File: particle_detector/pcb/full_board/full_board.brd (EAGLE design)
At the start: 32 x 64 mm, 39 parts, among them IC1 LT1807R, IC2 ATTINY5, IC3 LT3461, IC5 SENSL-SIPM

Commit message: Change ATTiny pads to save space
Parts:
- IC1: device personal:SO8 -> Personal:SO8
- IC2: device personal:PDIP8 -> Personal:PDIP8
- IC3: device personal:SOT23-6 -> Personal:SOT23-6
- IC5: device personal:MICROFC-60035 -> Personal:MICROFC-60035
- XBUS1, XBUS2: device personal:XBUS_2X05_PAD -> Personal:XBUS_2X05_PAD
- moved IC2 0.96 mm to (-8.45, 43.3)
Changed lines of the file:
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@@
 <attribute name="PROD_ID" value="DIO-09886" x="29.65" y="68" size="1.778" layer="27" rot="R90" display="off"/>
 </element>
-<element name="IC1" library="personal" package="SO8" package3d_urn="urn:adsk.eagle:package:3906/1" value="LT1807R" x="21.35" y="59" smashed="yes" rot="R270">
+<element name="IC1" library="Personal" package="SO8" package3d_urn="urn:adsk.eagle:package:3906/1" value="LT1807R" x="21.35" y="59" smashed="yes" rot="R270">
 <attribute name="MF" value="ALTERA CORPORATION" x="21.35" y="59" size="1.778" layer="27" rot="R270" display="off"/>
 <attribute name="MPN" value="AD746JRZ" x="21.35" y="59" size="1.778" layer="27" rot="R270" display="off"/>
@@
 <attribute name="VALUE" x="21.745" y="57.045" size="0.6" layer="27" font="vector" rot="R90"/>
 </element>
-<element name="IC3" library="personal" package="SOT23-6" value="LT3461" x="9.65" y="52.6" smashed="yes" rot="R270">
+<element name="IC3" library="Personal" package="SOT23-6" value="LT3461" x="9.65" y="52.6" smashed="yes" rot="R270">
 <attribute name="VALUE" x="8.095" y="49.421" size="0.6" layer="27" font="vector"/>
 </element>
@@
 <attribute name="VALUE" x="27.94" y="71.28" size="0.6" layer="27" font="vector" rot="R90"/>
 </element>
-<element name="XBUS1" library="personal" package="XBUS_2X05_PAD" value="" x="16" y="46.85" smashed="yes">
+<element name="XBUS1" library="Personal" package="XBUS_2X05_PAD" value="" x="16" y="46.85" smashed="yes">
 <attribute name="VALUE" x="11.92" y="43.675" size="1.27" layer="27"/>
 </element>
-<element name="L1" library="rcl" library_urn="urn:adsk.eagle:library:334" package="L3225M" package3d_urn="urn:adsk.eagle:package:23477/1" value="47uH" x="9.6" y="58.2" smashed="yes" rot="R90">
+<element name="L1" library="rcl" library_urn="urn:adsk.eagle:library:334" package="L3225M" package3d_urn="urn:adsk.eagle:package:23477/2" value="47uH" x="9.6" y="58.2" smashed="yes" rot="R90">
 <attribute name="NAME" x="7.695" y="60.805" size="0.6" layer="25" font="vector"/>
+<attribute name="POPULARITY" value="11" x="9.6" y="58.2" size="1.778" layer="27" rot="R90" display="off"/>
 <attribute name="SPICEPREFIX" value="L" x="9.6" y="58.2" size="1.778" layer="27" rot="R90" display="off"/>
 <attribute name="VALUE" x="8.795" y="60.825" size="0.6" layer="27" font="vector"/>
 </element>
-<element name="IC5" library="personal" package="MICROFC-60035" value="SENSL-SIPM" x="16" y="91.35" smashed="yes" rot="R180"/>
+<element name="IC5" library="Personal" package="MICROFC-60035" value="SENSL-SIPM" x="16" y="91.35" smashed="yes" rot="R180"/>
 <element name="C12" library="rcl" package="C0805K" value="10uF" x="13" y="66" smashed="yes">
 <attribute name="NAME" x="11.2" y="66.975" size="0.6" layer="25" font="vector"/>
@@
 <attribute name="VALUE" x="11.84" y="73.83" size="0.6" layer="27" font="vector" rot="R90"/>
 </element>
-<element name="XBUS2" library="personal" package="XBUS_2X05_PAD" value="" x="28.6" y="59.35" smashed="yes" rot="R270">
+<element name="XBUS2" library="Personal" package="XBUS_2X05_PAD" value="" x="28.6" y="59.35" smashed="yes" rot="R270">
 <attribute name="VALUE" x="25.425" y="63.43" size="1.27" layer="27" rot="R270"/>
 </element>
@@
 <attribute name="VALUE" x="28.33" y="69.825" size="1.27" layer="27"/>
 </element>
-<element name="IC2" library="personal" package="PDIP8" value="ATTINY5" x="-7.7" y="43.9" smashed="yes">
-<attribute name="NAME" x="-10.24" y="51.012" size="1.27" layer="25"/>
-<attribute name="VALUE" x="-10.748" y="35.518" size="1.27" layer="27"/>
+<element name="IC2" library="Personal" package="PDIP8" value="ATTINY5" x="-8.45" y="43.3" smashed="yes">
+<attribute name="NAME" x="-10.99" y="50.412" size="1.27" layer="25"/>
+<attribute name="VALUE" x="-11.498" y="34.918" size="1.27" layer="27"/>
 </element>
 </elements>
@@
 <wire x1="29.75" y1="45.6" x2="27.4" y2="52.8" width="0" layer="19" extent="1-1"/>
 <wire x1="2.25" y1="45.6" x2="8.35" y2="52.6" width="0" layer="19" extent="1-1"/>
-<wire x1="-11.256" y1="40.09" x2="2.25" y2="45.6" width="0" layer="19" extent="1-1"/>
+<wire x1="-12.006" y1="39.49" x2="2.25" y2="45.6" width="0" layer="19" extent="1-1"/>
 <wire x1="2.25" y1="105.1" x2="28" y2="103.35" width="0" layer="19" extent="1-1"/>
 </signal>
@@
 <wire x1="24.6637" y1="48.6637" x2="21.0156" y2="48.6637" width="0.2" layer="1"/>
 <contactref element="IC2" pad="P5"/>
-<wire x1="-3.636" y1="40.09" x2="18" y2="46.85" width="0" layer="19" extent="1-1"/>
+<wire x1="-4.386" y1="39.49" x2="18" y2="46.85" width="0" layer="19" extent="1-1"/>
 </signal>
 <signal name="SCL">
@@
 <wire x1="25.4024" y1="59.367925" x2="25.4024" y2="61.8024" width="0.2" layer="1"/>
 <contactref element="IC2" pad="P7"/>
-<wire x1="-3.636" y1="45.17" x2="20" y2="46.85" width="0" layer="19" extent="1-1"/>
+<wire x1="-4.386" y1="44.57" x2="20" y2="46.85" width="0" layer="19" extent="1-1"/>
 </signal>
 <signal name="N$6">
@@
 <wire x1="24.3" y1="58.8" x2="26" y2="60.5" width="0.2" layer="16"/>
 <contactref element="IC2" pad="P2"/>
-<wire x1="-11.256" y1="45.17" x2="11.62" y2="52.38" width="0" layer="19" extent="16-16"/>
+<wire x1="-12.006" y1="44.57" x2="11.62" y2="52.38" width="0" layer="19" extent="16-16"/>
 </signal>
 <signal name="TX">
@@
 <wire x1="23.7963" y1="50.3356" x2="22.1244" y2="48.6637" width="0.2" layer="16"/>
 <contactref element="IC2" pad="P3"/>
-<wire x1="-11.256" y1="42.63" x2="5" y2="53.54" width="0" layer="19" extent="16-16"/>
+<wire x1="-12.006" y1="42.03" x2="5" y2="53.54" width="0" layer="19" extent="16-16"/>
 </signal>
 <signal name="5V">
@@
 <wire x1="25.45" y1="63.35" x2="23.95" y2="60.905" width="0" layer="19" extent="1-1"/>
 <wire x1="13.84" y1="49.84" x2="10.95" y2="51.65" width="0" layer="19" extent="1-1"/>
-<wire x1="-3.636" y1="47.71" x2="7.2" y2="57.2" width="0" layer="19" extent="1-1"/>
+<wire x1="-4.386" y1="47.11" x2="7.2" y2="57.2" width="0" layer="19" extent="1-1"/>
 </signal>
 <signal name="N$10">
 <contactref element="R10" pad="2"/>
 <contactref element="IC2" pad="P6"/>
-<wire x1="-3.636" y1="42.63" x2="24.55" y2="73.95" width="0" layer="19" extent="1-1"/>
+<wire x1="-4.386" y1="42.03" x2="24.55" y2="73.95" width="0" layer="19" extent="1-1"/>
 </signal>
 </signals>

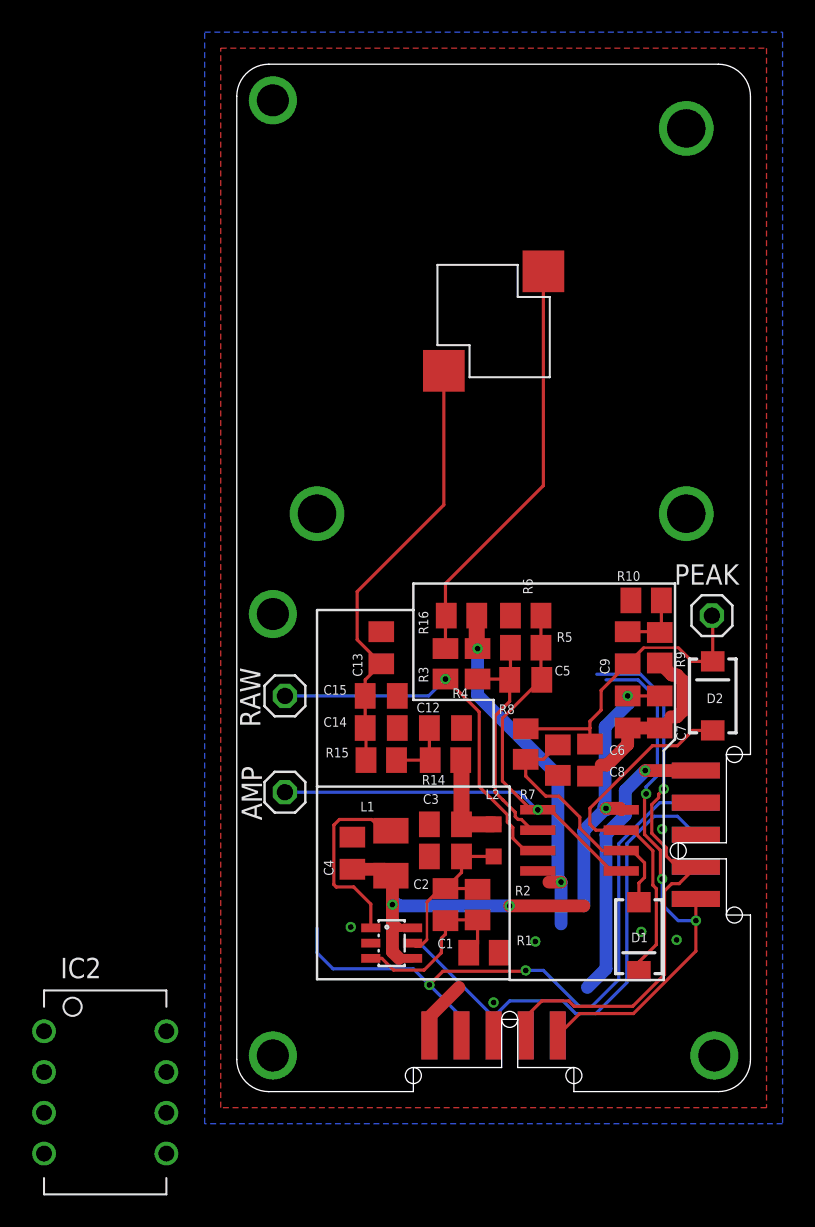
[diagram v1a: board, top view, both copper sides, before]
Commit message: complete a draft of the circuit layout
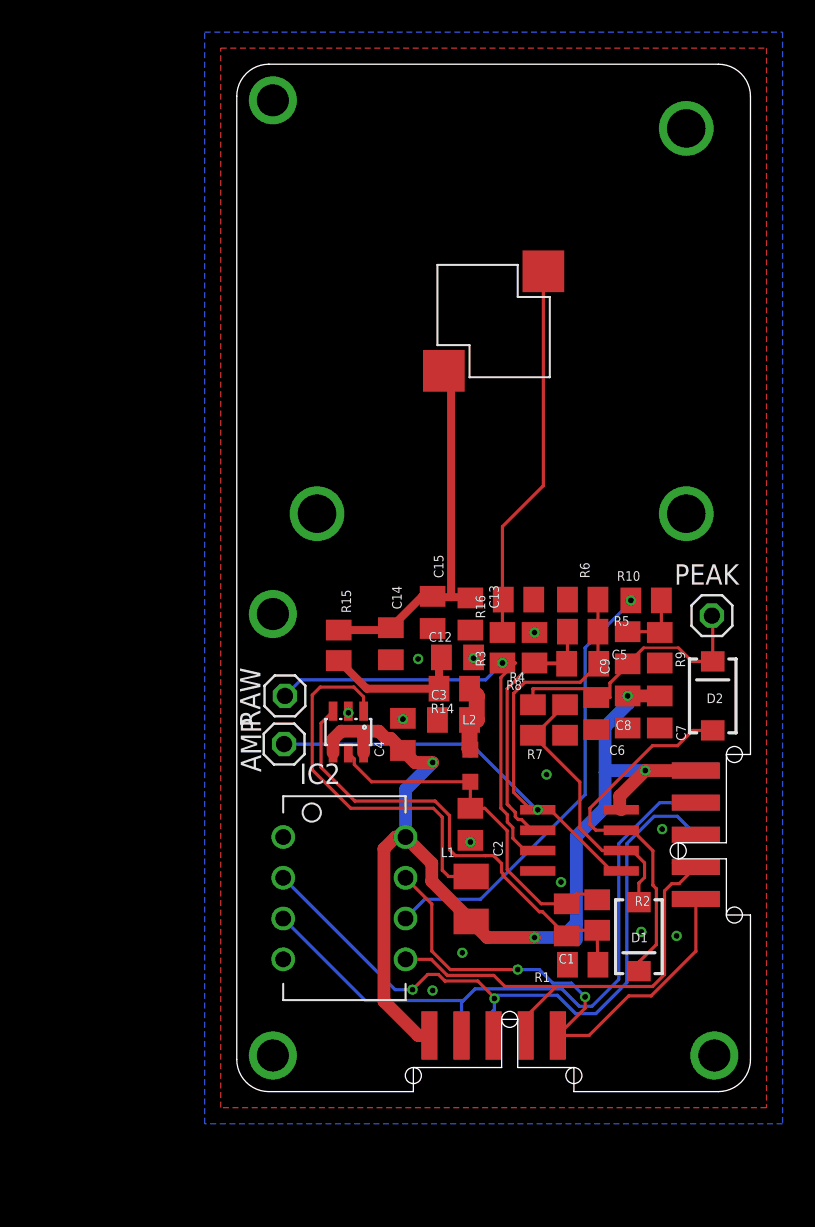
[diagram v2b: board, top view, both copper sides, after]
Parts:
- moved IC2 19.2 mm to (6.45, 55.4)
- moved IC3 13.4 mm to (6.95, 65.8), turned to 180 degrees
- moved C4 8.04 mm to (10.3, 65.6)
- moved R15 7.63 mm to (6.35, 71.2), turned to 90 degrees
- moved C1 7.61 mm to (20.6, 54.0)
- moved R2 7.48 mm to (22.4, 54.4)
- moved C3 6.52 mm to (13.5, 66.5)
- moved R1 6.20 mm to (21.6, 51.2), turned to 0 degrees
- moved C15 6.11 mm to (12.2, 73.2), turned to 270 degrees
- moved C13 5.93 mm to (14.6, 73.1), turned to 270 degrees
- moved L1 5.76 mm to (14.6, 55.4)
- moved C14 5.28 mm to (9.60, 71.2), turned to 270 degrees
- moved L2 4.87 mm to (14.6, 63.6)
- moved R14 4.48 mm to (13.6, 68.5)
- moved C12 4.46 mm to (13.8, 70.4)
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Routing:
- net GND: track 32.0 -> 0.07 mm, vias 15 -> 20
- net N$10: track 0.00 -> 27.8 mm, vias 0 -> 1
- net N$3: track 11.5 -> 29.3 mm
- net RX: track 31.3 -> 43.3 mm, vias 0 -> 2
- net N$1: track 12.0 -> 23.8 mm
- net N$7: track 11.4 -> 22.5 mm
- net 5V: track 61.4 -> 71.4 mm, vias 5 -> 4
- net SDA: track 36.4 -> 30.3 mm, vias 1 -> 0
- net SIG_AMP: track 37.3 -> 42.5 mm
- net N$11: track 4.12 -> 9.20 mm
- net SIG_RAW: track 24.0 -> 28.7 mm
- net N$8: track 15.3 -> 18.5 mm
- net N$6: track 27.5 -> 24.7 mm
- net SIGNAL: track 26.1 -> 23.6 mm
- net HV: track 6.02 -> 4.46 mm
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
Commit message: Reorganize trace lengths to shorten distances
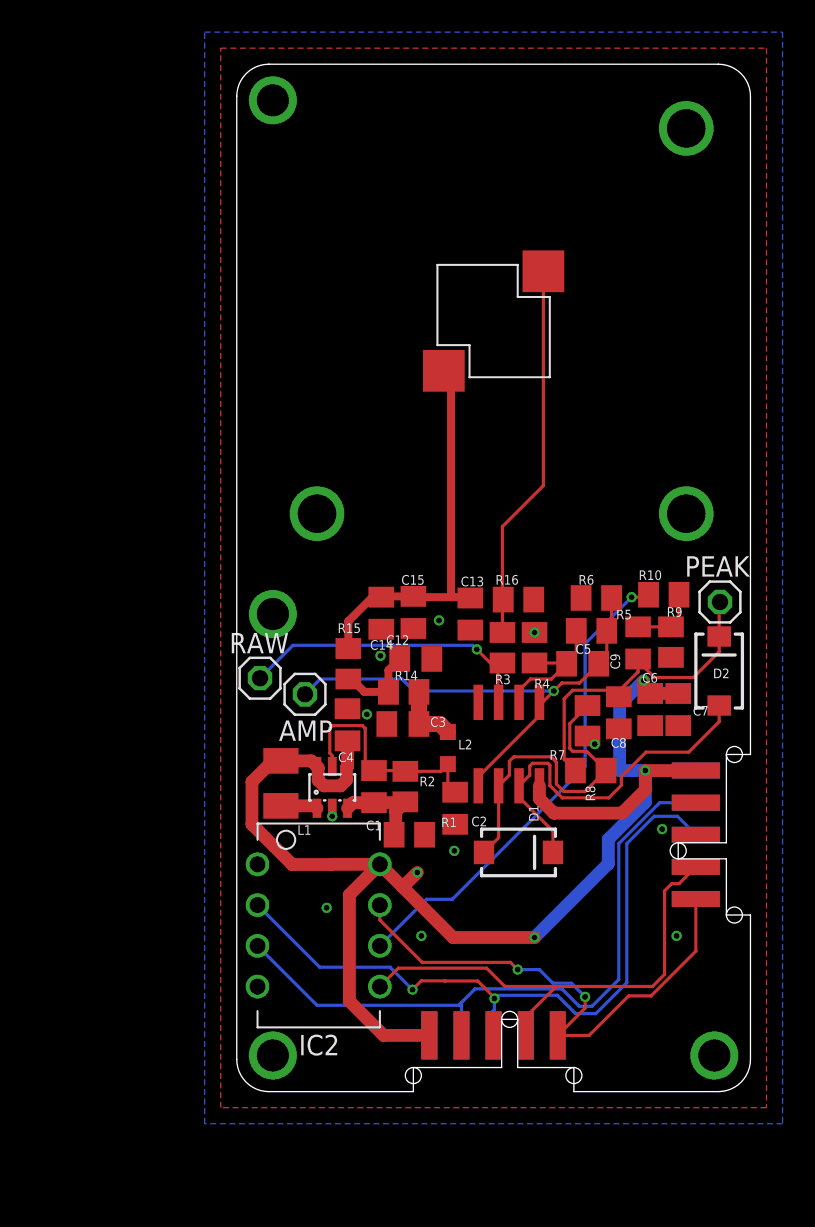
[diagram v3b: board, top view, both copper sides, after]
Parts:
- moved C1 14.6 mm to (8.55, 62.4)
- moved R2 14.4 mm to (10.5, 62.4)
- moved L1 13.9 mm to (2.75, 62.5), turned to 270 degrees
- moved R1 13.5 mm to (10.8, 59.4), turned to 180 degrees
- moved D1 9.15 mm to (17.6, 58.2), turned to 0 degrees
- moved IC1 7.44 mm to (16.9, 65.0), turned to 180 degrees
- moved R8 4.78 mm to (22.1, 63.4), turned to 180 degrees
- moved IC3 3.59 mm to (5.95, 62.3), turned to 0 degrees
- moved C4 3.50 mm to (6.90, 66.2)
- moved AMP 3.36 mm to (4.25, 68.1)
- moved C3 3.16 mm to (10.3, 66.2)
- moved R14 3.16 mm to (10.4, 68.2)
- moved C12 2.60 mm to (11.2, 70.3)
- moved IC2 2.33 mm to (4.85, 53.7)
- moved C14 1.99 mm to (9.00, 73.2)
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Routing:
- net N$3: track 29.3 -> 6.11 mm
- net N$1: track 23.8 -> 2.31 mm
- net 5V: track 71.4 -> 86.5 mm
- net SIG_AMP: track 42.5 -> 32.2 mm
- net N$8: track 18.5 -> 8.68 mm
- net SIG_RAW: track 28.7 -> 19.0 mm
- net N$7: track 22.5 -> 14.4 mm
- net N$11: track 9.20 -> 5.38 mm
- net SIG_PEAK: track 17.5 -> 21.2 mm
- net N$4: track 18.2 -> 20.8 mm
- net N$10: track 27.8 -> 30.3 mm
- net SDA: track 30.3 -> 32.1 mm
- net TX: track 41.0 -> 42.0 mm
- net N$6: track 24.7 -> 25.5 mm
- net RX: track 43.3 -> 43.9 mm
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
